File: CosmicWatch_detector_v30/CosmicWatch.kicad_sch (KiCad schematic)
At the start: 111 parts, among them J3 RJ45, P1 CONN_01X04, P10 CONN_02X02, P11 CONN_01X01, P12 CONN_01X01, P13 CONN_01X01, P14 CONN_01X01, P15 CONN_02X04, P16 CONN_01X02, P19 CONN_01X01, P2 CONN_01X01, P29 CONN_01X01, P3 CONN_01X04, P30 CONN_01X01, P32 CONN_01X04, P4 CONN_01X04, P5 CONN_01X02, P7 CONN_01X01, P8 CONN_01X01, SW1 RESET, U1 LT3461, U10 SiPM_AFBR-S4N33C013, U12 LTC6752, U13 TS5A1066, U16 UMCC, U17 UMCC, U19 LMH6658, U2 SiPM_MicroFJ−300XX−TSV, U22 UMCC, U23 UMCC, U3 MMCX, U4 TS5A1066, U5 RasberryPi_Pico, U6 LMH6658, U7 TPS6040X, U8 sd_card_socket, U9 2NPNMBT6429DW1T1G

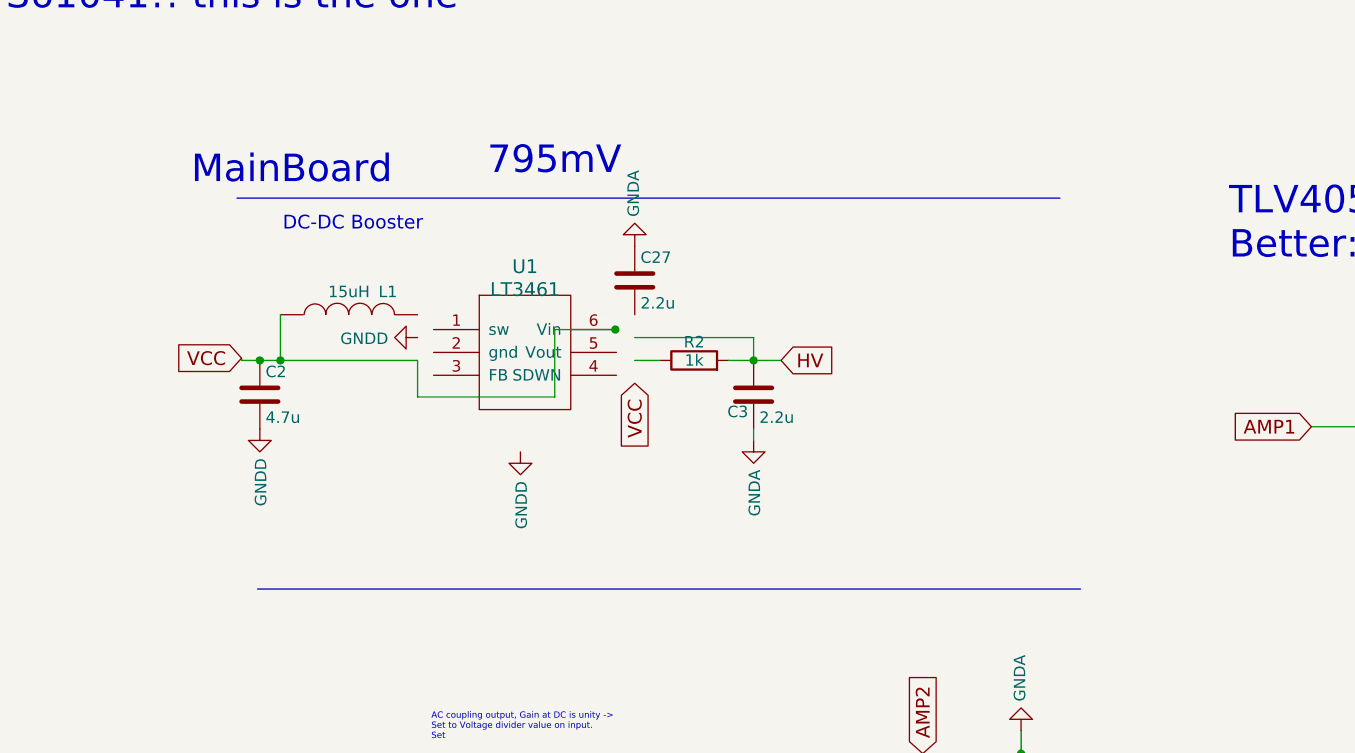
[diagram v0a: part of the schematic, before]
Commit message: adding DC-DC booster on v3 schematics and pcb
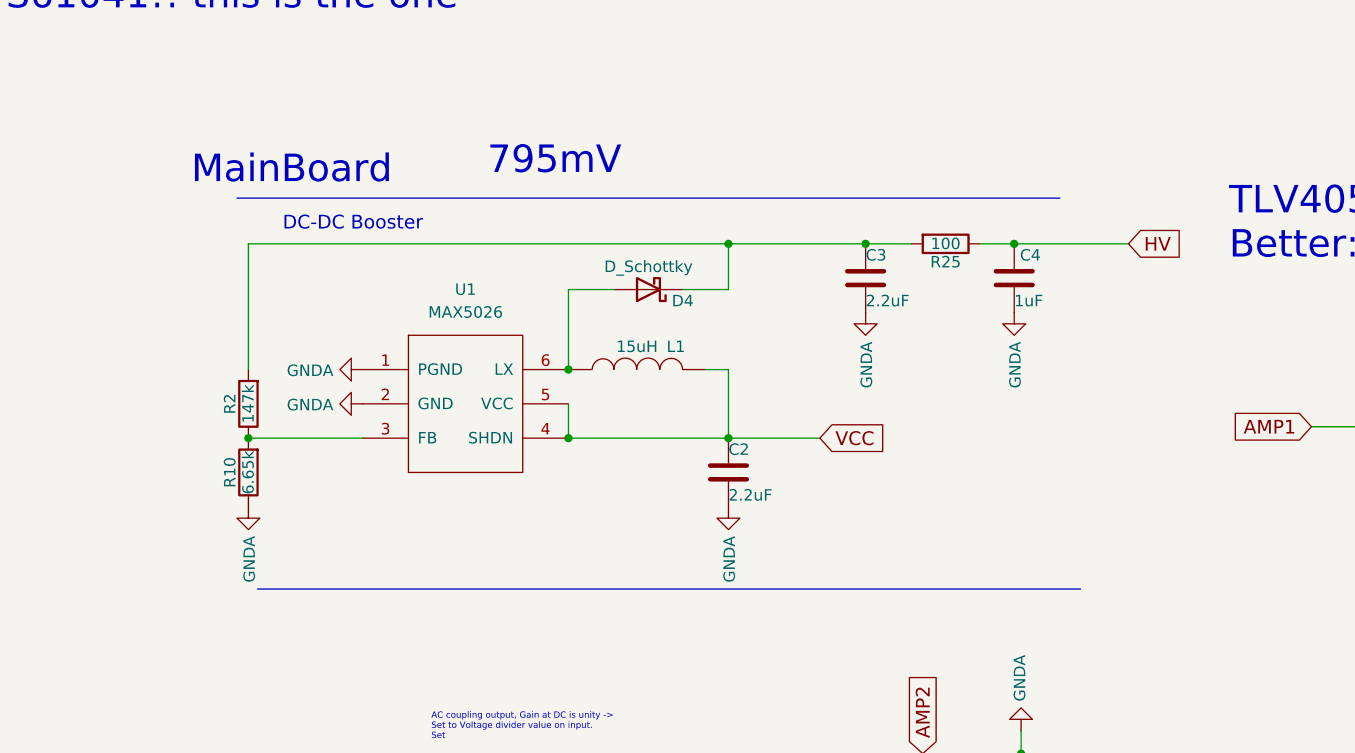
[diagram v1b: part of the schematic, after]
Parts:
- removed C2: 4.7u, Capacitor_SMD:C_1206_3216Metric, symbol device:C
- removed C27: 2.2u, Capacitor_SMD:C_0603_1608Metric, symbol device:C
- removed C3: 2.2u, Capacitor_SMD:C_1206_3216Metric, symbol device:C
- removed U1: LT3461, Package_TO_SOT_SMD:SOT-23-6_Handsoldering, symbol MyLibrary:LT3461
- added C2, C3: 2.2uF, Capacitor_SMD:C_1206_3216Metric, symbol Device:C
- added C4: 1uF, Capacitor_SMD:C_0603_1608Metric, symbol device:C
- added D4: D_Schottky, Diode_SMD:D_SOD-523, symbol My_Symbol_Library:D_Schottky
- added R10: 6.65k, Capacitor_SMD:C_0603_1608Metric, symbol device:R
- added R25: 100, Capacitor_SMD:C_0603_1608Metric, symbol device:R
- added U1: MAX5026, Package_TO_SOT_SMD:SOT-23-6_Handsoldering, symbol My_Symbol_Library:MAX5026
- R2: value 1k -> 147k
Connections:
- net GNDA: now also C2.2, C3.2, C4.2, R10.1, U1.1 (PGND), U1.2 (GND)
- net HV: now also C4.1, R25.1; no longer R2.2
- net VCC: now also L1.2, C2.1, U1.4 (SHDN), U1.5 (VCC); no longer L1.1
- net at R2.1: now also R10.2, U1.3 (FB)
- new net: C3.1, D4.1 (K), R2.2, R25.2
- new net: D4.2 (A), L1.1, U1.6 (LX)

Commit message: rearranging DC-DC booster components
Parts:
- added C7: 0.1uF, Capacitor_SMD:C_0603_1608Metric, symbol device:C
- C2: value 2.2uF -> 10uF
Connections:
- net GNDA: now also C7.2
- net VCC: now also C7.1
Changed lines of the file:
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@@
   (junction (at 27.94 55.88) (diameter 0) (color 0 0 0 0)
   )
+  (junction (at 68.834 55.88) (diameter 0) (color 0 0 0 0)
+  )
   (junction (at 63.5 48.26) (diameter 0) (color 0 0 0 0)
   )
@@
     (stroke (width 0) (type default))
   )
+  (wire (pts (xy 68.834 55.88) (xy 81.28 55.88))
+    (stroke (width 0) (type default))
+  )
   (wire (pts (xy 53.34 205.74) (xy 58.42 205.74))
     (stroke (width 0) (type default))
@@
     (stroke (width 0) (type default))
   )
+  (wire (pts (xy 63.5 55.88) (xy 68.834 55.88))
+    (stroke (width 0) (type default))
+  )
   (wire (pts (xy 367.03 25.4) (xy 368.554 25.4))
     (stroke (width 0) (type default))
@@
     (stroke (width 0) (type default))
   )
-  (wire (pts (xy 63.5 55.88) (xy 81.28 55.88))
-    (stroke (width 0) (type default))
-  )
   (wire (pts (xy 131.445 162.56) (xy 127.635 162.56))
     (stroke (width 0) (type default))
@@
     )
   )
+  (symbol (lib_id "power:GNDA") (at 68.834 63.5 0) (unit 1)
+    (in_bom yes) (on_board yes) (dnp no)
+    (property "Reference" "#PWR015" (at 68.834 69.85 0)
+      (effects (font (size 1.27 1.27)) hide)
+    )
+    (property "Value" "GNDA" (at 68.961 66.7512 90)
+      (effects (font (size 1.27 1.27)) (justify right))
+    )
+    (property "Footprint" "" (at 68.834 63.5 0)
+      (effects (font (size 1.27 1.27)))
+    )
+    (property "Datasheet" "" (at 68.834 63.5 0)
+      (effects (font (size 1.27 1.27)))
+    )
+    (pin "1")
+    (instances
+      (project "CosmicWatch"
+        (path "/4ba73f5d-b469-4168-abd4-8f6ff03fbc45"
+          (reference "#PWR015") (unit 1)
+        )
+      )
+      (project "DC-DC-booster"
+        (path "/ee3fefaa-818f-4207-9a53-d175ff74ab66"
+          (reference "#PWR04") (unit 1)
+        )
+      )
+    )
+  )
   (symbol (lib_id "power:GNDA") (at 27.94 63.5 0) (unit 1)
     (in_bom yes) (on_board yes) (dnp no)
@@
       (effects (font (size 1.27 1.27)) (justify left))
     )
-    (property "Value" "2.2uF" (at 81.28 62.23 0)
+    (property "Value" "10uF" (at 81.28 62.23 0)
       (effects (font (size 1.27 1.27)) (justify left))
     )
@@
         )
       )
+    )
+  )
+  (symbol (lib_id "device:C") (at 68.834 59.69 0) (unit 1)
+    (in_bom yes) (on_board yes) (dnp no)
+    (property "Reference" "C7" (at 69.469 57.15 0)
+      (effects (font (size 1.27 1.27)) (justify left))
+    )
+    (property "Value" "0.1uF" (at 69.596 61.976 0)
+      (effects (font (size 1.27 1.27)) (justify left))
+    )
+    (property "Footprint" "Capacitor_SMD:C_0603_1608Metric" (at 69.7992 63.5 0)
+      (effects (font (size 1.27 1.27)) hide)
+    )
+    (property "Datasheet" "" (at 68.834 59.69 0)
+      (effects (font (size 1.27 1.27)))
+    )
+    (pin "1")
+    (pin "2")
+    (instances
+      (project "CosmicWatch"
+        (path "/4ba73f5d-b469-4168-abd4-8f6ff03fbc45"
+          (reference "C7") (unit 1)
+        )
+      )

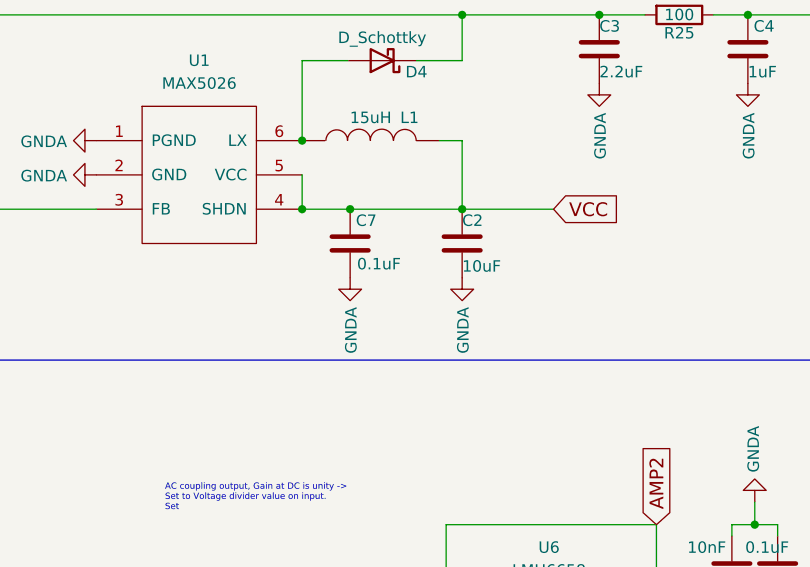
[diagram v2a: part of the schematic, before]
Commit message: new booster added
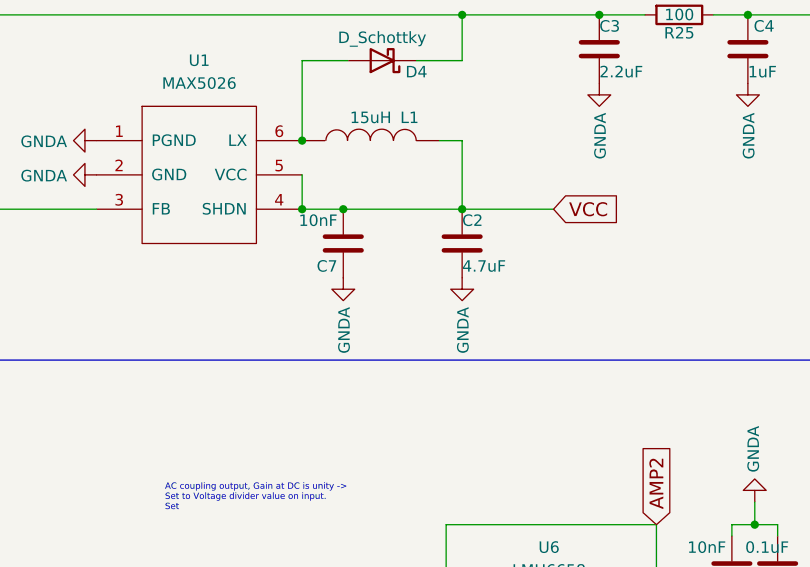
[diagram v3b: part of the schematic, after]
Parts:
- C2: value 10uF -> 4.7uF
- C7: value 0.1uF -> 10nF
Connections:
- net GNDA: now also C7.1; no longer C7.2
- net VCC: now also C7.2; no longer C7.1
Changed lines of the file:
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@@
   (junction (at 27.94 55.88) (diameter 0) (color 0 0 0 0)
   )
-  (junction (at 68.834 55.88) (diameter 0) (color 0 0 0 0)
-  )
   (junction (at 63.5 48.26) (diameter 0) (color 0 0 0 0)
   )
@@
   (junction (at 130.302 102.362) (diameter 0) (color 0 0 0 0)
   )
+  (junction (at 68.072 55.88) (diameter 0) (color 0 0 0 0)
+  )
   (junction (at 142.748 102.362) (diameter 0) (color 0 0 0 0)
   )
@@
     (stroke (width 0) (type default))
   )
-  (wire (pts (xy 68.834 55.88) (xy 81.28 55.88))
-    (stroke (width 0) (type default))
-  )
   (wire (pts (xy 53.34 205.74) (xy 58.42 205.74))
     (stroke (width 0) (type default))
@@
     (stroke (width 0) (type default))
   )
+  (wire (pts (xy 68.072 55.88) (xy 81.28 55.88))
+    (stroke (width 0) (type default))
+  )
   (wire (pts (xy 79.502 99.822) (xy 79.502 98.552))
     (stroke (width 0) (type default))
@@
     (stroke (width 0) (type default))
   )
-  (wire (pts (xy 63.5 55.88) (xy 68.834 55.88))
+  (wire (pts (xy 63.5 55.88) (xy 68.072 55.88))
     (stroke (width 0) (type default))
   )
@@
     )
   )
-  (symbol (lib_id "power:GNDA") (at 68.834 63.5 0) (unit 1)
+  (symbol (lib_id "power:GNDA") (at 68.072 63.5 0) (unit 1)
     (in_bom yes) (on_board yes) (dnp no)
-    (property "Reference" "#PWR015" (at 68.834 69.85 0)
+    (property "Reference" "#PWR015" (at 68.072 69.85 0)
       (effects (font (size 1.27 1.27)) hide)
     )
-    (property "Value" "GNDA" (at 68.961 66.7512 90)
+    (property "Value" "GNDA" (at 68.199 66.7512 90)
       (effects (font (size 1.27 1.27)) (justify right))
     )
-    (property "Footprint" "" (at 68.834 63.5 0)
+    (property "Footprint" "" (at 68.072 63.5 0)
       (effects (font (size 1.27 1.27)))
     )
-    (property "Datasheet" "" (at 68.834 63.5 0)
+    (property "Datasheet" "" (at 68.072 63.5 0)
       (effects (font (size 1.27 1.27)))
     )
@@
     )
   )
+  (symbol (lib_id "device:C") (at 68.072 59.69 180) (unit 1)
+    (in_bom yes) (on_board yes) (dnp no)
+    (property "Reference" "C7" (at 67.437 62.23 0)
+      (effects (font (size 1.27 1.27)) (justify left))
+    )
+    (property "Value" "10nF" (at 67.437 57.15 0)
+      (effects (font (size 1.27 1.27)) (justify left))
+    )
+    (property "Footprint" "Capacitor_SMD:C_0603_1608Metric" (at 67.1068 55.88 0)
+      (effects (font (size 1.27 1.27)) hide)
+    )
+    (property "Datasheet" "" (at 68.072 59.69 0)
+      (effects (font (size 1.27 1.27)))
+    )
+    (pin "1")
+    (pin "2")
+    (instances
+      (project "CosmicWatch"
+        (path "/4ba73f5d-b469-4168-abd4-8f6ff03fbc45"
+          (reference "C7") (unit 1)
+        )
+      )
+    )
+  )
   (symbol (lib_id "device:R") (at 108.077 102.362 270) (unit 1)
     (in_bom yes) (on_board yes) (dnp no)
@@
       (effects (font (size 1.27 1.27)) (justify left))
     )
-    (property "Value" "10uF" (at 81.28 62.23 0)
+    (property "Value" "4.7uF" (at 81.28 62.23 0)
       (effects (font (size 1.27 1.27)) (justify left))
     )
@@
         )
       )
-    )
-  )
-  (symbol (lib_id "device:C") (at 68.834 59.69 0) (unit 1)
-    (in_bom yes) (on_board yes) (dnp no)
-    (property "Reference" "C7" (at 69.469 57.15 0)
-      (effects (font (size 1.27 1.27)) (justify left))
-    )
-    (property "Value" "0.1uF" (at 69.596 61.976 0)
-      (effects (font (size 1.27 1.27)) (justify left))
-    )
-    (property "Footprint" "Capacitor_SMD:C_0603_1608Metric" (at 69.7992 63.5 0)
-      (effects (font (size 1.27 1.27)) hide)
-    )
-    (property "Datasheet" "" (at 68.834 59.69 0)
-      (effects (font (size 1.27 1.27)))
-    )
-    (pin "1")
-    (pin "2")
-    (instances
-      (project "CosmicWatch"
-        (path "/4ba73f5d-b469-4168-abd4-8f6ff03fbc45"
-          (reference "C7") (unit 1)
-        )
-      )

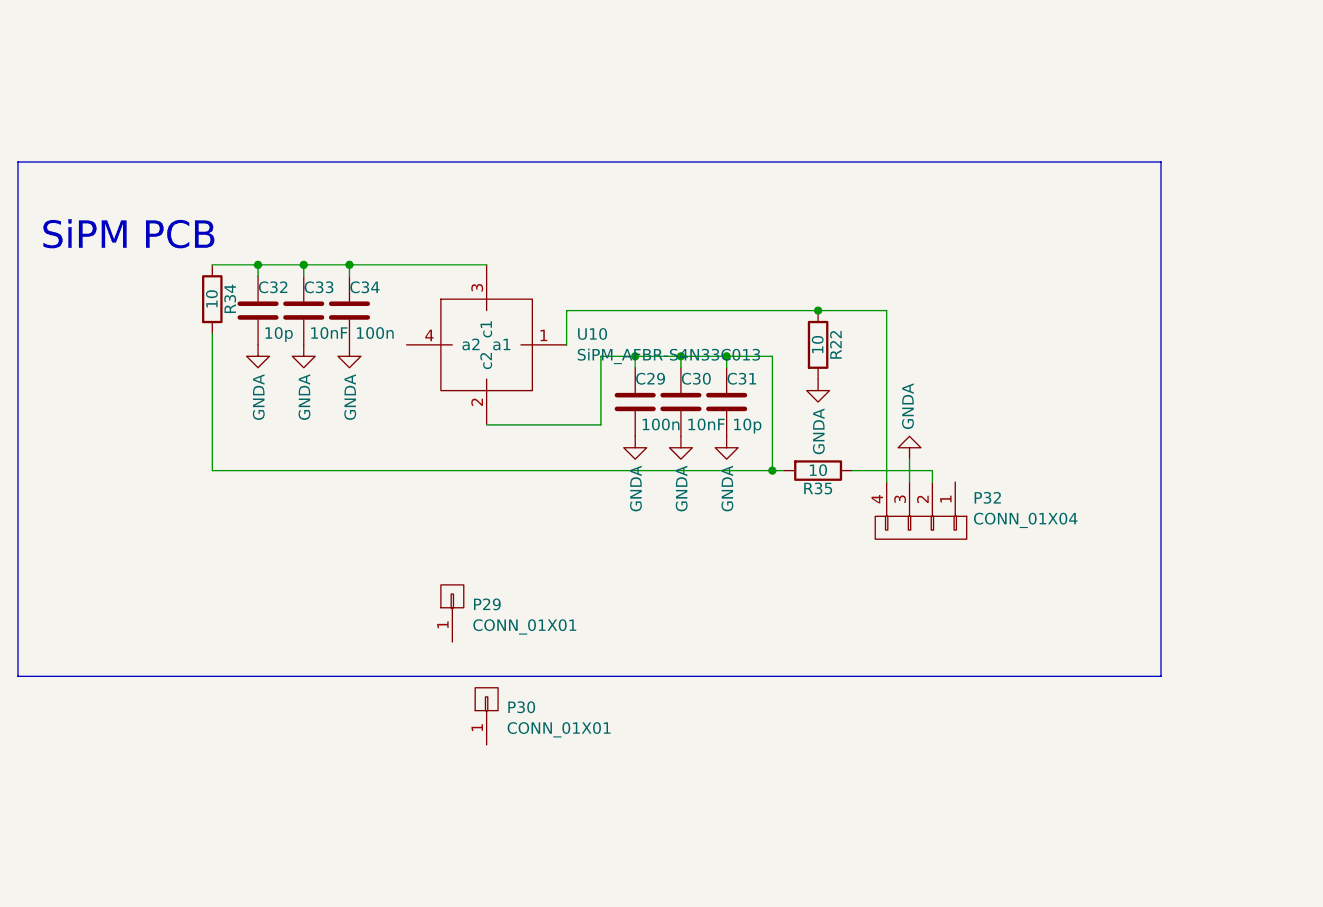
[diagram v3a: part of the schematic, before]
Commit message: removing second sipm
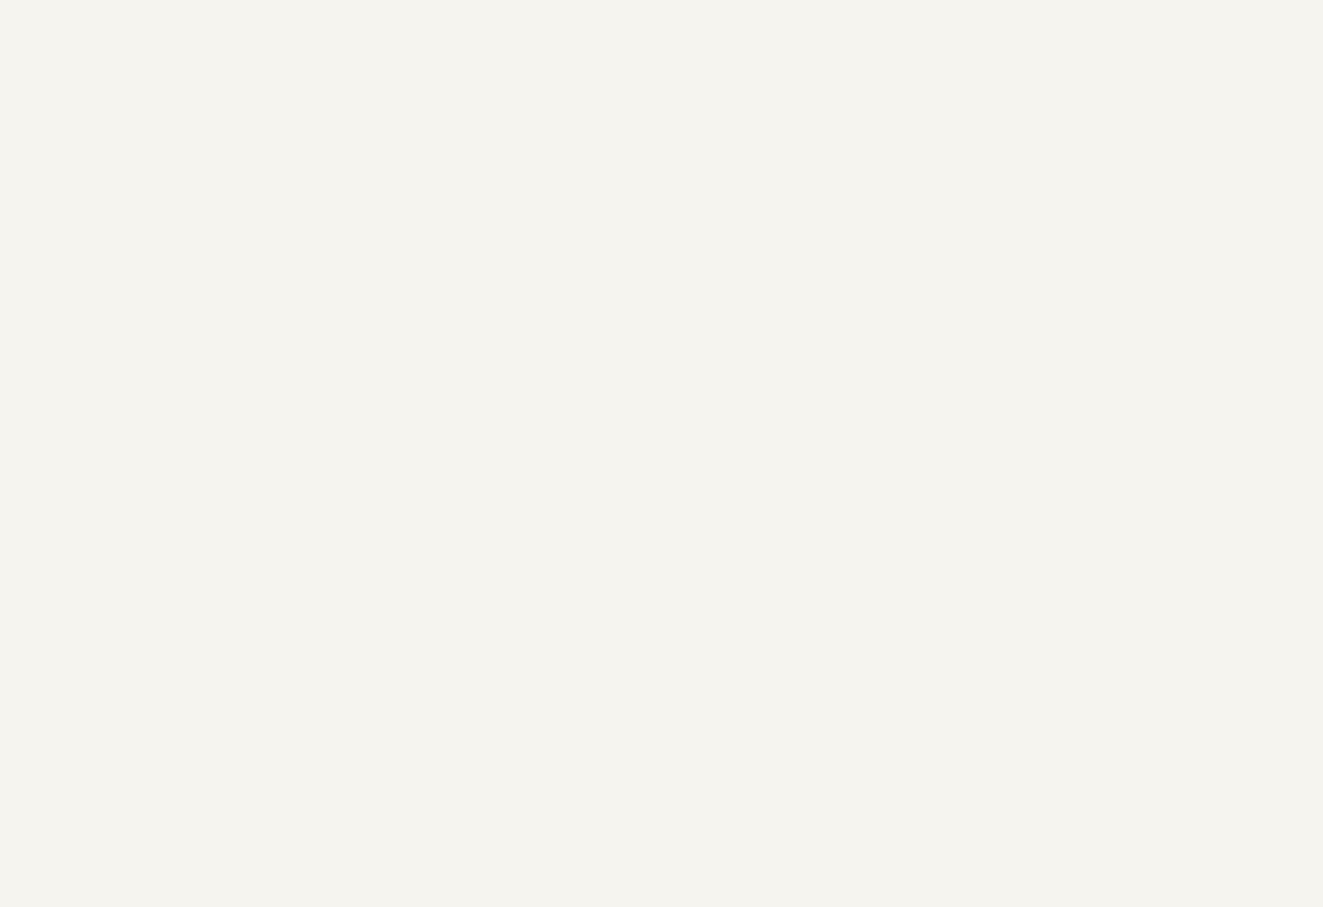
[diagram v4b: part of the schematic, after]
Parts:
- removed C29, C34: 100n, Capacitor_SMD:C_0603_1608Metric, symbol device:C
- removed C30, C33: 10nF, Capacitor_SMD:C_0603_1608Metric, symbol device:C
- removed C31, C32: 10p, Capacitor_SMD:C_0603_1608Metric, symbol device:C
- removed P29, P30: CONN_01X01, Connector_PinHeader_2.54mm:PinHeader_1x01_P2.54mm_Vertical, symbol conn:CONN_01X01
- removed P32: CONN_01X04, Connector_PinHeader_2.54mm:PinHeader_1x04_P2.54mm_Vertical, symbol conn:CONN_01X04
- removed R22, R34, R35: 10, Capacitor_SMD:C_0603_1608Metric, symbol device:R
- removed U10: SiPM_AFBR-S4N33C013, MyFootprints:SiPM_S4N33C013, symbol MyLibrary:SiPM_AFBR-S4N33C013
